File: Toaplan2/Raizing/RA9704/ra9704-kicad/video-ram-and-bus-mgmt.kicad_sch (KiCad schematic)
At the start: 16 parts, among them U118 74AC14, U617 74HC244, U618 74HC244, U619 74HC244, U622 74HC244, U623 VVEC2_3A (MACH211), U624 A11235, U68 CY7C199, U69 CY7C199, X61 27 MHz

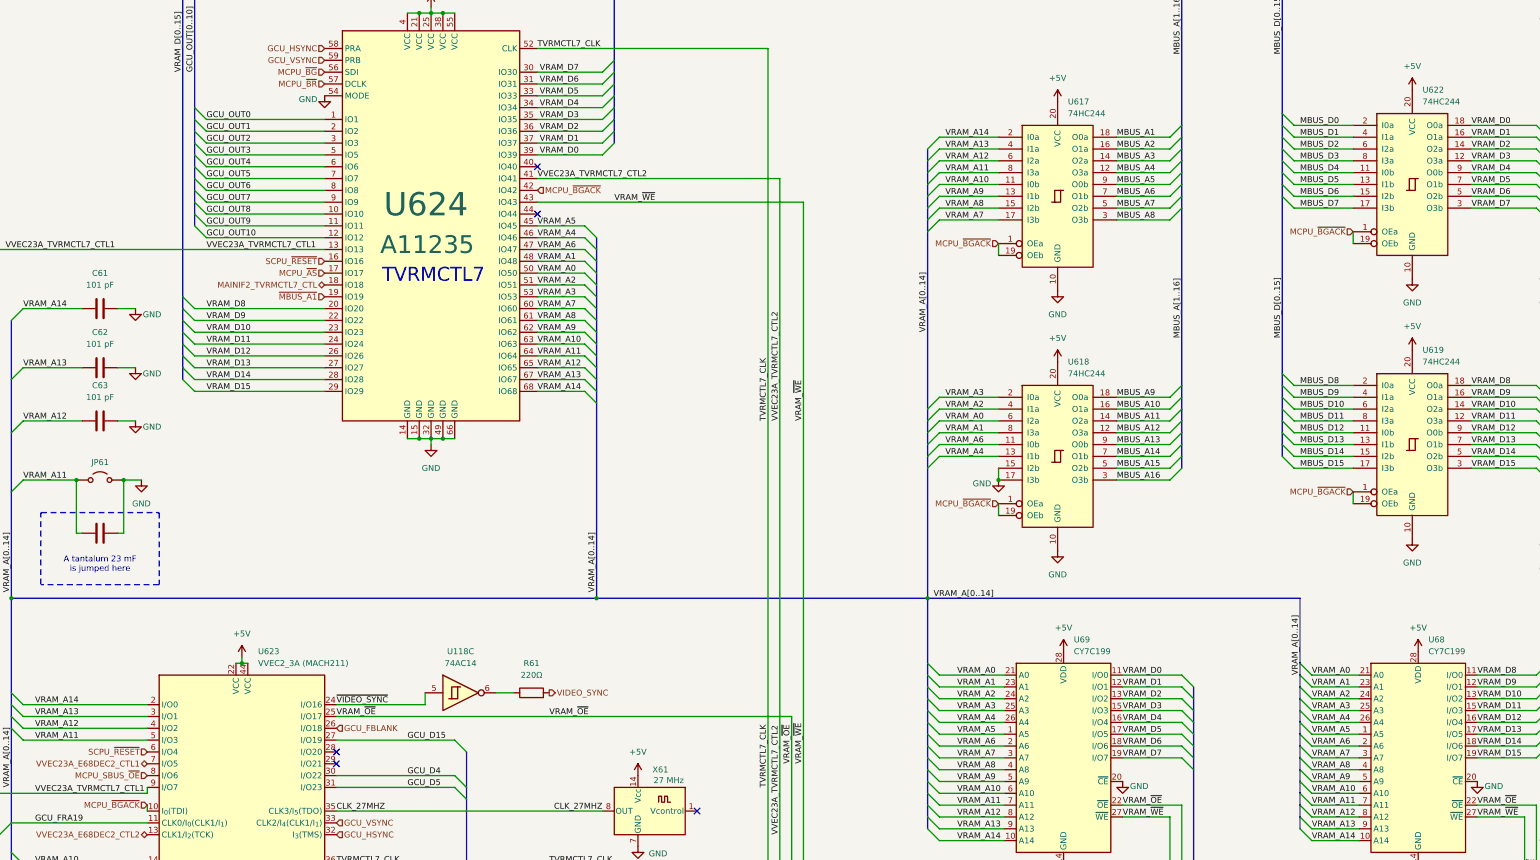
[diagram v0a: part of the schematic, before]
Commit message: fix(ra9704): Add Os as a proxy for 0s in all reference designators
RA9704 has reference designators such that each number has a preceding zero (e.g. RA076, U074, etc.). This causes a bug in KiCAD.

This is 'fixed' by using the 'O' (the letter 'Oh') character instead.

For more info, see the following issue on the KiCAD Gitlab repo

https://gitlab.com/kicad/code/kicad/-/issues/19229
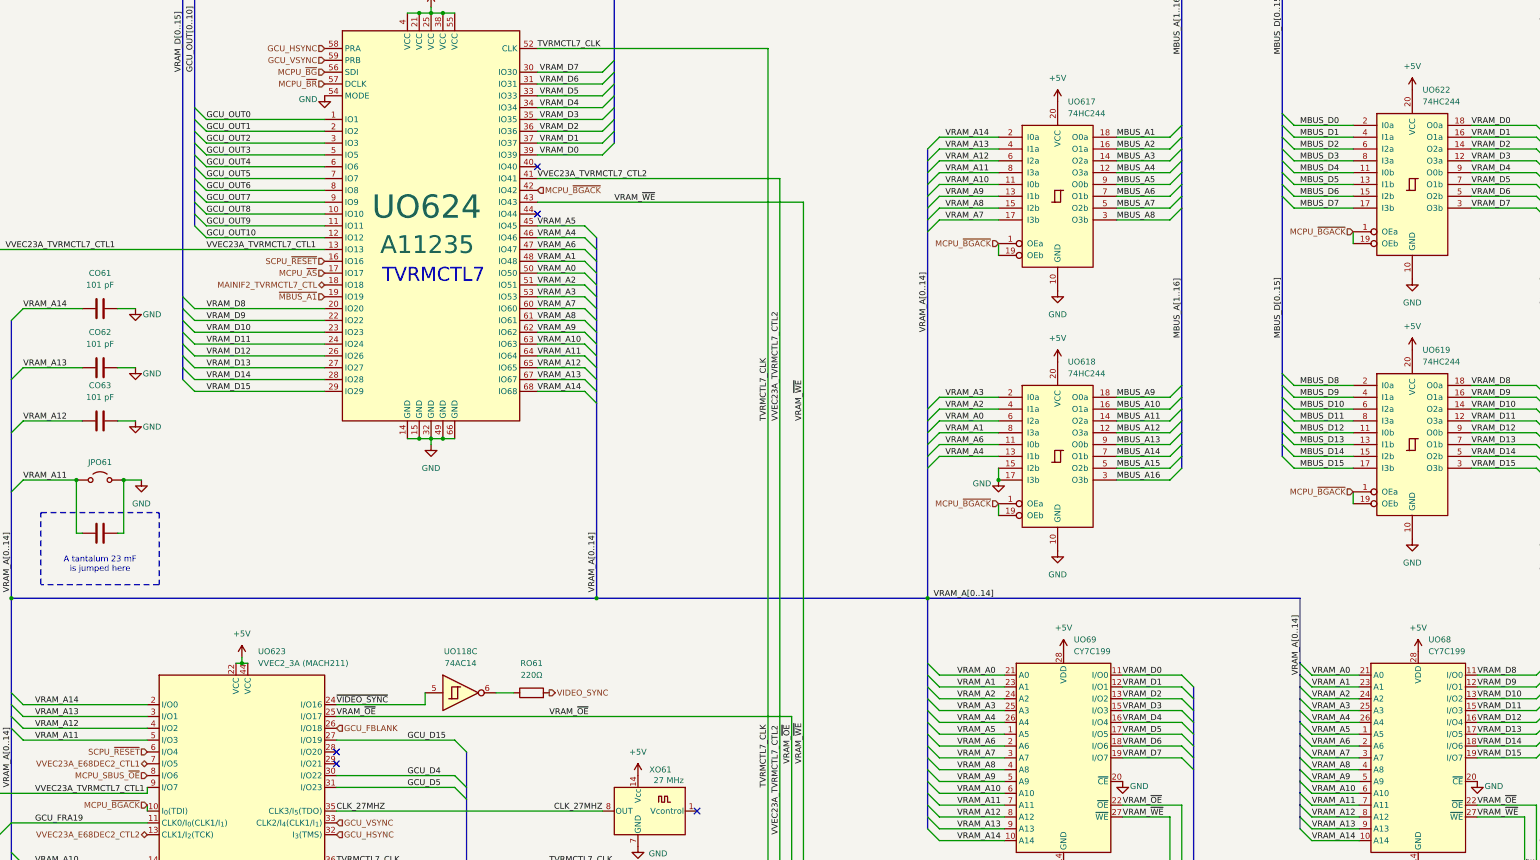
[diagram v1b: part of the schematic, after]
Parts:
- renumbered C61 to CO61, C62 to CO62, C63 to CO63, JP61 to JPO61, R61 to RO61, U118 to UO118, U617 to UO617, U618 to UO618, U619 to UO619, U622 to UO622, U623 to UO623, U624 to UO624, U68 to UO68, U69 to UO69, X61 to XO61
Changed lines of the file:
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@@
 		(dnp no)
 		(fields_autoplaced yes)
-		(property "Reference" "U118"
+		(property "Reference" "UO118"
 			(at 165.1 167.64 0)
 			(effects
@@
 			(project "ra9704"
 				(path "/24d3b4cf-2360-45fc-8c40-cedc8afdf9e1/7e3f3952-fdac-4324-a754-c9025bb7f3ca"
-					(reference "U118")
+					(reference "UO118")
 					(unit 3)
 				)
@@
 		(on_board yes)
 		(dnp no)
-		(property "Reference" "JP61"
+		(property "Reference" "JPO61"
 			(at 87.63 127 0)
 			(effects
@@
 			(project "ra9704"
 				(path "/24d3b4cf-2360-45fc-8c40-cedc8afdf9e1/7e3f3952-fdac-4324-a754-c9025bb7f3ca"
-					(reference "JP61")
+					(reference "JPO61")
 					(unit 1)
 				)
@@
 		(dnp no)
 		(fields_autoplaced yes)
-		(property "Reference" "C63"
+		(property "Reference" "CO63"
 			(at 87.63 110.49 90)
 			(effects
@@
 			(project "ra9704"
 				(path "/24d3b4cf-2360-45fc-8c40-cedc8afdf9e1/7e3f3952-fdac-4324-a754-c9025bb7f3ca"
-					(reference "C63")
+					(reference "CO63")
 					(unit 1)
 				)
@@
 		(dnp no)
 		(fields_autoplaced yes)
-		(property "Reference" "U622"
+		(property "Reference" "UO622"
 			(at 371.7641 46.99 0)
 			(effects
@@
 			(project "ra9704"
 				(path "/24d3b4cf-2360-45fc-8c40-cedc8afdf9e1/7e3f3952-fdac-4324-a754-c9025bb7f3ca"
-					(reference "U622")
+					(reference "UO622")
 					(unit 1)
 				)
@@
 		(dnp no)
 		(fields_autoplaced yes)
-		(property "Reference" "U618"
+		(property "Reference" "UO618"
 			(at 295.5641 105.41 0)
 			(effects
@@
 			(project "ra9704"
 				(path "/24d3b4cf-2360-45fc-8c40-cedc8afdf9e1/7e3f3952-fdac-4324-a754-c9025bb7f3ca"
-					(reference "U618")
+					(reference "UO618")
 					(unit 1)
 				)
@@
 		(dnp no)
 		(fields_autoplaced yes)
-		(property "Reference" "C62"
+		(property "Reference" "CO62"
 			(at 87.63 99.06 90)
 			(effects
@@
 			(project "ra9704"
 				(path "/24d3b4cf-2360-45fc-8c40-cedc8afdf9e1/7e3f3952-fdac-4324-a754-c9025bb7f3ca"
-					(reference "C62")
+					(reference "CO62")
 					(unit 1)
 				)
@@
 		(dnp no)
 		(fields_autoplaced yes)
-		(property "Reference" "U69"
+		(property "Reference" "UO69"
 			(at 296.8341 165.1 0)
 			(effects
@@
 			(project "ra9704"
 				(path "/24d3b4cf-2360-45fc-8c40-cedc8afdf9e1/7e3f3952-fdac-4324-a754-c9025bb7f3ca"
-					(reference "U69")
+					(reference "UO69")
 					(unit 1)
 				)
@@
 		(dnp no)
 		(fields_autoplaced yes)
-		(property "Reference" "U68"
+		(property "Reference" "UO68"
 			(at 373.0341 165.1 0)
 			(effects
@@
 			(project "ra9704"
 				(path "/24d3b4cf-2360-45fc-8c40-cedc8afdf9e1/7e3f3952-fdac-4324-a754-c9025bb7f3ca"
-					(reference "U68")
+					(reference "UO68")
 					(unit 1)
 				)
@@
 		(dnp no)
 		(fields_autoplaced yes)
-		(property "Reference" "U623"
+		(property "Reference" "UO623"
 			(at 121.5741 167.64 0)
 			(effects
@@
 			(project "ra9704"
 				(path "/24d3b4cf-2360-45fc-8c40-cedc8afdf9e1/7e3f3952-fdac-4324-a754-c9025bb7f3ca"
-					(reference "U623")
+					(reference "UO623")
 					(unit 1)
 				)
@@
 		(dnp no)
 		(fields_autoplaced yes)
-		(property "Reference" "U617"
+		(property "Reference" "UO617"
 			(at 295.5641 49.53 0)
 			(effects
@@
 			(project "ra9704"
 				(path "/24d3b4cf-2360-45fc-8c40-cedc8afdf9e1/7e3f3952-fdac-4324-a754-c9025bb7f3ca"
-					(reference "U617")
+					(reference "UO617")
 					(unit 1)
 				)
@@
 		(on_board yes)
 		(dnp no)
-		(property "Reference" "X61"
+		(property "Reference" "XO61"
 			(at 208.026 193.04 0)
 			(effects
@@
 			(project "ra9704"
 				(path "/24d3b4cf-2360-45fc-8c40-cedc8afdf9e1/7e3f3952-fdac-4324-a754-c9025bb7f3ca"
-					(reference "X61")
+					(reference "XO61")
 					(unit 1)
 				)
@@
 		(on_board yes)
 		(dnp no)
-		(property "Reference" "U624"
-			(at 148.59 71.628 0)
+		(property "Reference" "UO624"
+			(at 146.05 72.136 0)
 			(effects
 				(font
@@
 			(project "ra9704"
 				(path "/24d3b4cf-2360-45fc-8c40-cedc8afdf9e1/7e3f3952-fdac-4324-a754-c9025bb7f3ca"
-					(reference "U624")
+					(reference "UO624")
 					(unit 1)
 				)
@@
 		(dnp no)
 		(fields_autoplaced yes)
-		(property "Reference" "U619"
+		(property "Reference" "UO619"
 			(at 371.7641 102.87 0)
 			(effects
@@
 			(project "ra9704"
 				(path "/24d3b4cf-2360-45fc-8c40-cedc8afdf9e1/7e3f3952-fdac-4324-a754-c9025bb7f3ca"
-					(reference "U619")
+					(reference "UO619")
 					(unit 1)
 				)
@@
 		(dnp no)
 		(fields_autoplaced yes)
-		(property "Reference" "R61"
+		(property "Reference" "RO61"
 			(at 180.34 170.18 90)
 			(effects
@@
 			(project "ra9704"
 				(path "/24d3b4cf-2360-45fc-8c40-cedc8afdf9e1/7e3f3952-fdac-4324-a754-c9025bb7f3ca"
-					(reference "R61")
+					(reference "RO61")
 					(unit 1)
 				)
@@
 		(dnp no)
 		(fields_autoplaced yes)
-		(property "Reference" "C61"
+		(property "Reference" "CO61"
 			(at 87.63 86.36 90)
 			(effects
@@
 			(project "ra9704"
 				(path "/24d3b4cf-2360-45fc-8c40-cedc8afdf9e1/7e3f3952-fdac-4324-a754-c9025bb7f3ca"
-					(reference "C61")
-					(unit 1)
-				)
+					(reference "CO61")
+					(unit 1)
+				)
